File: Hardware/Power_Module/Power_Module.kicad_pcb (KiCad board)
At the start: 2 copper layers, 1 part, among them IC1 MAX17301G+

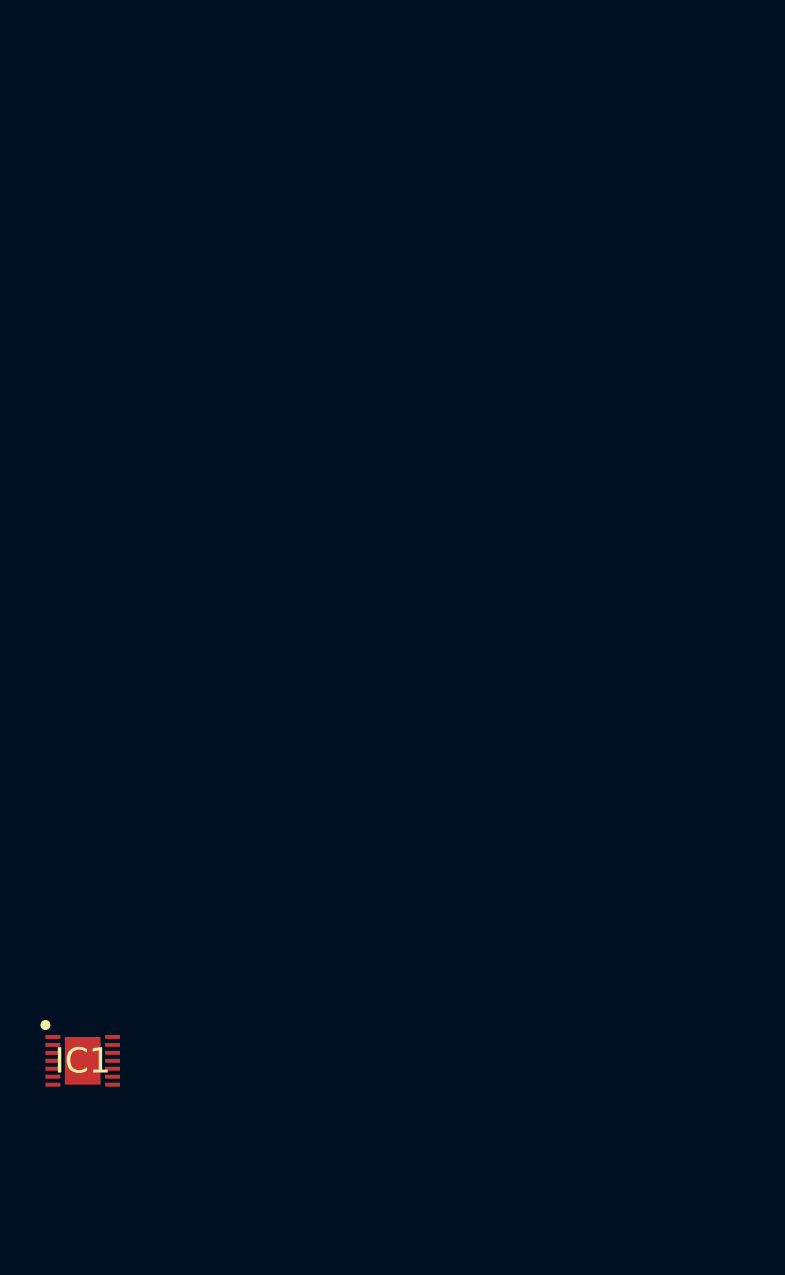
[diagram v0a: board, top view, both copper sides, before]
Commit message: Added power module pcb
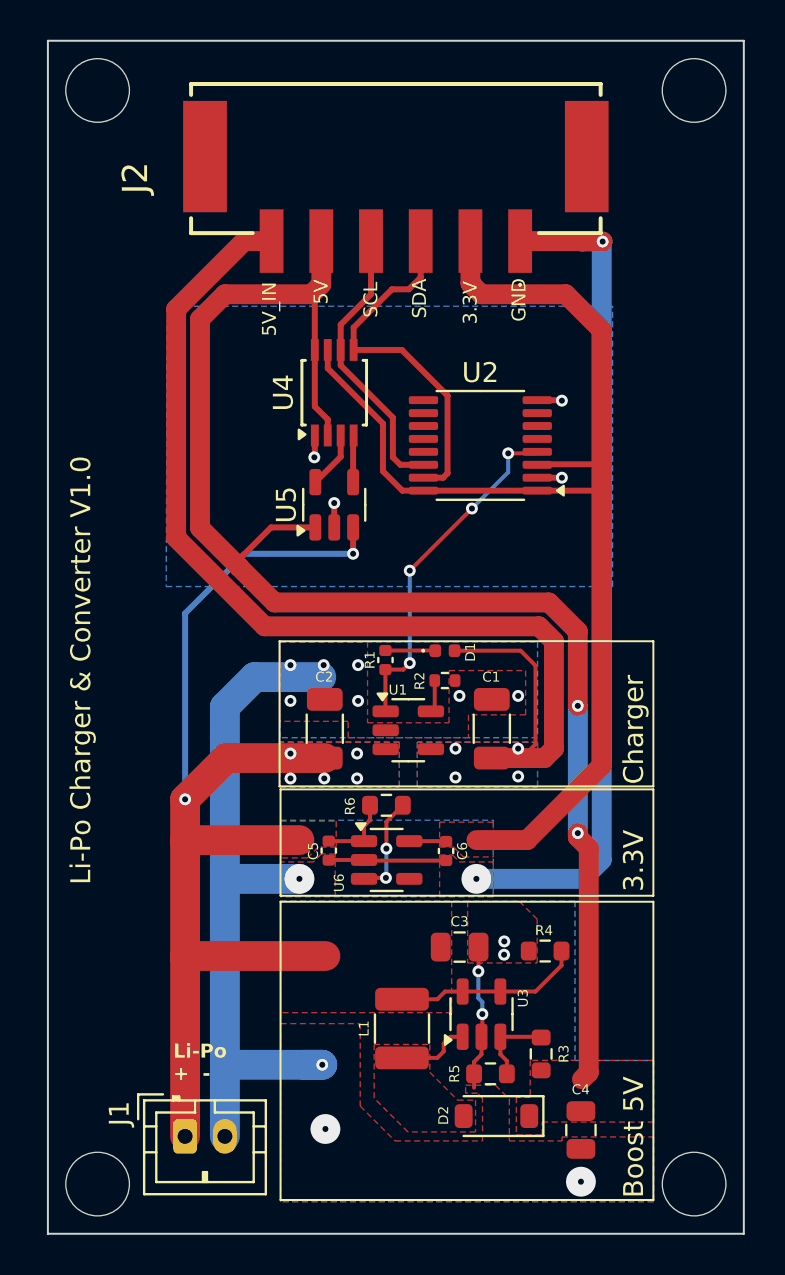
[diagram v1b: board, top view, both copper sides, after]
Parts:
- removed IC1: MAX17301G+, MAX17301G+:SON40P300X300X80-15N
- added C1: 4.7uF 6V, Capacitor_SMD:C_1206_3216Metric, F.Cu at (107.1, 55.6)
- added C2: 4.7uF 6V, Capacitor_SMD:C_1206_3216Metric, F.Cu at (98.7, 55.6)
- added C3: 4.7uF 6.3V, Capacitor_SMD:C_0805_2012Metric, F.Cu at (105.5, 66.6)
- added C4: 22uF 6.3V, Capacitor_SMD:C_0805_2012Metric, F.Cu at (111.6, 75.8)
- added C5: 1uF, Capacitor_SMD:C_0402_1005Metric, F.Cu at (98.9, 61.7)
- added C6: 1uF, Capacitor_SMD:C_0402_1005Metric, F.Cu at (104.8, 61.8)
- added D1: LED, LED_SMD:LED_0402_1005Metric, F.Cu at (104.7, 51.7)
- added D2: MBRM140T3G, Diode_SMD:D_SOD-123, F.Cu at (107.3, 75.1)
- added J1: B2B-PH-K-SLFSN, Connector_JST:JST_PH_B2B-PH-K_1x02_P2.00mm_Vertical, F.Cu at (91.7, 76.1)
- added J2: 1814951, footprints:1814951, F.Cu at (102.2, 27.9)
- added L1: 4.7uH 650mA, Capacitor_SMD:C_1210_3225Metric, F.Cu at (102.6, 70.7)
- added R1: 634, Capacitor_SMD:C_0402_1005Metric, F.Cu at (101.7, 52.1)
- added R2: 2K, Resistor_SMD:R_0402_1005Metric, F.Cu at (104.7, 53.2)
- added R3: 5.62KΩ, Resistor_SMD:R_0603_1608Metric, F.Cu at (109.6, 72.0)
- added R4: 10KΩ, Resistor_SMD:R_0603_1608Metric, F.Cu at (109.8, 66.8)
- added R5: 1.87KΩ, Resistor_SMD:R_0603_1608Metric, F.Cu at (107.0, 73.0)
- added R6: 10KΩ, Resistor_SMD:R_0603_1608Metric, F.Cu at (101.8, 59.5)
- added U1: MCP73832-2-OT, Package_TO_SOT_SMD:SOT-23-5, F.Cu at (102.9, 55.7)
- added U2: PCA6408APW_118, Package_SO:TSSOP-16_4.4x5mm_P0.65mm, F.Cu at (106.5, 41.4)
- added U3: MIC2288YD5-TR, Package_TO_SOT_SMD:TSOT-23-5, F.Cu at (106.6, 70.0)
- added U4: ~, Package_SO:TSSOP-8_3x3mm_P0.65mm, F.Cu at (99.2, 38.7)
- added U5: MCP3021A2T-E/OT, Package_TO_SOT_SMD:TSOT-23-5, F.Cu at (99.2, 44.3)
- added U6: MIC5504-3.3YM5, Package_TO_SOT_SMD:SOT-23-5, F.Cu at (101.8, 62.2)
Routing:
- net GND: track 0.00 -> 96.9 mm, vias 0 -> 21
- net 5V: track 0.00 -> 76.4 mm, vias 0 -> 2
- net Vbat: track 0.00 -> 71.2 mm, vias 0 -> 7
- net 3.3V: track 0.00 -> 63.2 mm
- net 5V Charger: track 0.00 -> 58.4 mm, vias 0 -> 4
- net SDA 3.3V: track 0.00 -> 18.3 mm
- net Charging_Status: track 0.00 -> 17.6 mm, vias 0 -> 4
- net SCL 3.3V: track 0.00 -> 14.3 mm
- net Net-(U6-EN): track 0.00 -> 5.12 mm, vias 0 -> 2
- net Net-(U3-FB): track 0.00 -> 4.06 mm
- net Net-(U3-SW): track 0.00 -> 3.72 mm
- net Net-(U4-SCLA): track 0.00 -> 2.88 mm
- net Net-(D1-K): track 0.00 -> 2.51 mm
- net Net-(U4-SDAA): track 0.00 -> 2.36 mm
- net Net-(U1-PROG): track 0.00 -> 1.63 mm
- added copper zone on F.Cu, net 3.3V
- added copper zone on F.Cu, net 5V
- added copper zone on B.Cu, net 5V Charger
- added copper zone on F.Cu, net 5V Charger
- added copper zone on B.Cu, net GND
- added copper zone on F.Cu, net GND
- added copper zone on F.Cu, net Net-(U3-SW)
- added copper zone on B.Cu, net Vbat
- added copper zone on F.Cu, net Vbat
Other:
- board outline added: 35 x 60 mm
- board text added: "3.3V"
- board text added: "3.3V_OUT"
- board text added: "5V"
- board text added: "5V_IN"
- board text added: "5V_OUT"
- board text added: "Boost 5V"
- board text added: "Charger"
- board text added: "GND"
- board text added: "Li-Po + -"
- board text added: "Li-Po Charger & Converter V1.0"
- board text added: "SCL"
- board text added: "SCL_3.3V"
- board text added: "SDA"
- board text added: "SDA_3.3V"

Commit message: Added LED Matrix for fun
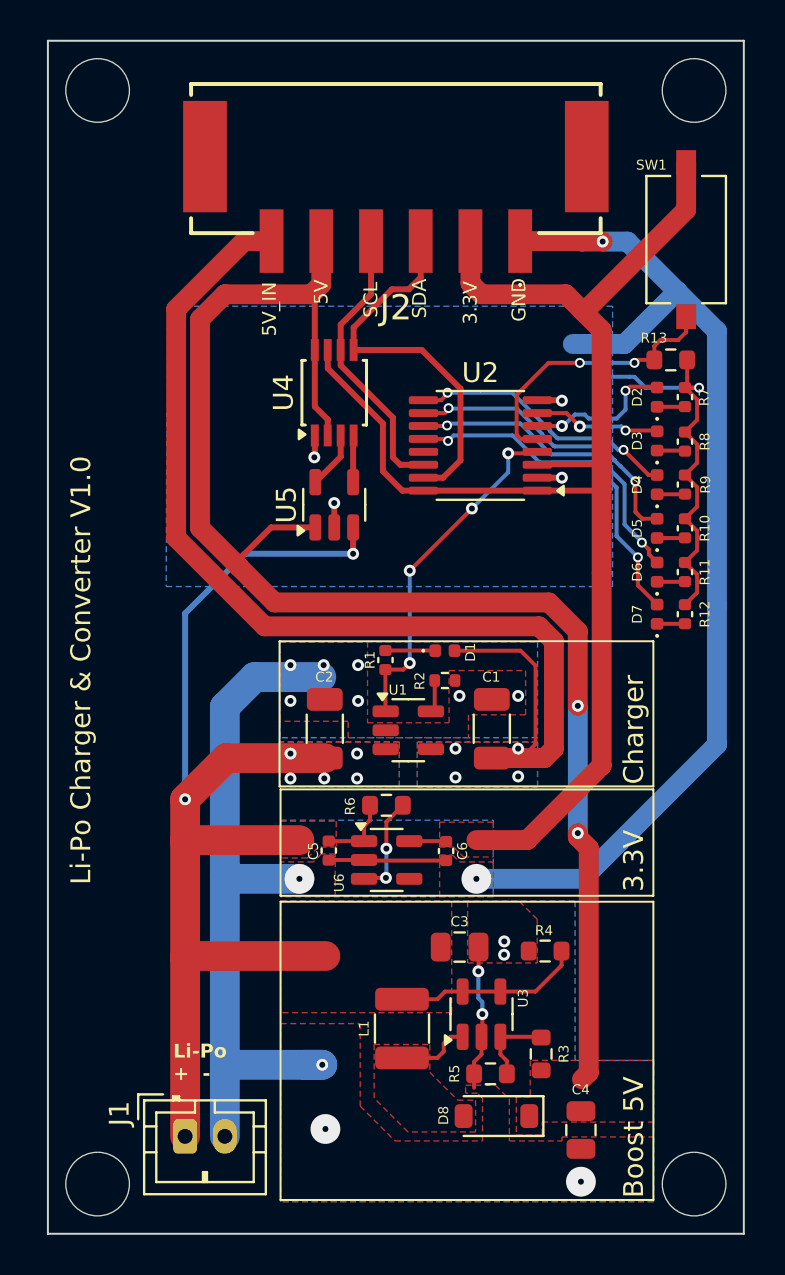
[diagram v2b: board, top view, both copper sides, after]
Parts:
- added D2: LED, LED_SMD:LED_0402_1005Metric, F.Cu at (115.4, 38.9)
- added D3: LED, LED_SMD:LED_0402_1005Metric, F.Cu at (115.4, 41.1)
- added D4: LED, LED_SMD:LED_0402_1005Metric, F.Cu at (115.4, 43.3)
- added D5: LED, LED_SMD:LED_0402_1005Metric, F.Cu at (115.4, 45.5)
- added D6: LED, LED_SMD:LED_0402_1005Metric, F.Cu at (115.4, 47.7)
- added D7: LED, LED_SMD:LED_0402_1005Metric, F.Cu at (115.4, 49.8)
- added R10: 634, Capacitor_SMD:C_0402_1005Metric, F.Cu at (116.8, 45.5)
- added R11: 634, Capacitor_SMD:C_0402_1005Metric, F.Cu at (116.8, 47.7)
- added R12: 634, Capacitor_SMD:C_0402_1005Metric, F.Cu at (116.8, 49.8)
- added R13: 10KΩ, Resistor_SMD:R_0603_1608Metric, F.Cu at (116.1, 37.0)
- added R7: 634, Capacitor_SMD:C_0402_1005Metric, F.Cu at (116.8, 38.9)
- added R8: 634, Capacitor_SMD:C_0402_1005Metric, F.Cu at (116.8, 41.2)
- added R9: 634, Capacitor_SMD:C_0402_1005Metric, F.Cu at (116.8, 43.3)
- added SW1: SW_Push, Button_Switch_SMD:SW_Tactile_SPST_NO_Straight_CK_PTS636Sx25SMTRLFS, F.Cu at (116.8, 31.0)
- C3: value 4.7uF 6.3V -> 10uF 6.3V
- C4: value 22uF 6.3V -> 10uF 6.3V
- J2: footprint footprints:1814951 -> Library:1814951
- renumbered D2 to D8
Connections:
- U2 pad 10: unconnected-(U2-P5-Pad10) -> Net-(D5-A)
- U2 pad 11: unconnected-(U2-P6-Pad11) -> Net-(D6-A)
- U2 pad 12: unconnected-(U2-P7-Pad12) -> Net-(D7-A)
- U2 pad 5: unconnected-(U2-P1-Pad5) -> Net-(U2-P1)
- U2 pad 6: unconnected-(U2-P2-Pad6) -> Net-(D2-A)
- U2 pad 7: unconnected-(U2-P3-Pad7) -> Net-(D3-A)
- U2 pad 9: unconnected-(U2-P4-Pad9) -> Net-(D4-A)
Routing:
- net GND: track 96.9 -> 129.0 mm, vias 21 -> 22
- net Net-(D7-A): track 0.00 -> 17.7 mm, vias 0 -> 2
- net Net-(D6-A): track 0.00 -> 16.1 mm, vias 0 -> 2
- net Net-(D5-A): track 0.00 -> 15.1 mm, vias 0 -> 2
- net Net-(U2-P1): track 0.00 -> 14.2 mm, vias 0 -> 2
- net Net-(D4-A): track 0.00 -> 13.8 mm, vias 0 -> 2
- net 3.3V: track 63.2 -> 72.9 mm
- net Net-(D2-A): track 0.00 -> 7.58 mm, vias 0 -> 2
- net Net-(D3-A): track 0.00 -> 6.41 mm, vias 0 -> 2
- net Net-(D3-K): track 0.00 -> 1.41 mm
- net Net-(D4-K): track 0.00 -> 1.40 mm
- net Net-(D6-K): track 0.00 -> 1.40 mm
- net Net-(D5-K): track 0.00 -> 1.40 mm
- net Net-(D2-K): track 0.00 -> 1.40 mm
- net Net-(D7-K): track 0.00 -> 1.40 mm
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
